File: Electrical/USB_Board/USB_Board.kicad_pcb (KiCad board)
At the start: 2 copper layers, 45 x 18 mm, 24 parts, among them J1 USB_B_Mini, Q1 BC850, Q2 BC850, U1 FT232RL, U2 AD8620

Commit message: Fixed hole size on ICSP board.
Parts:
- D1: footprint LED_SMD:LED_1206_3216Metric -> Diode_SMD:D_1206_3216Metric
- L4, L5: footprint Diode_SMD:D_1206_3216Metric -> LED_SMD:LED_1206_3216Metric

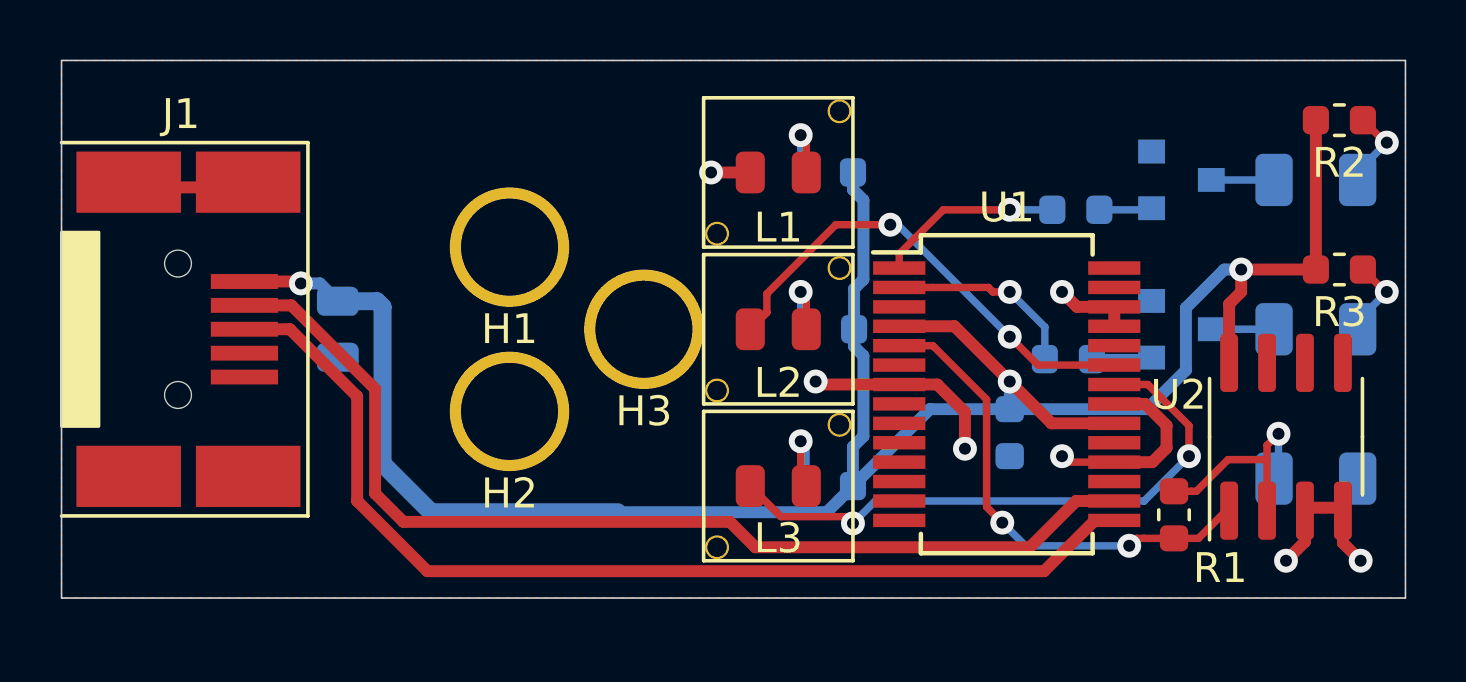
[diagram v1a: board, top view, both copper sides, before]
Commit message: Updated transimpedance amp and rearranged USB board.
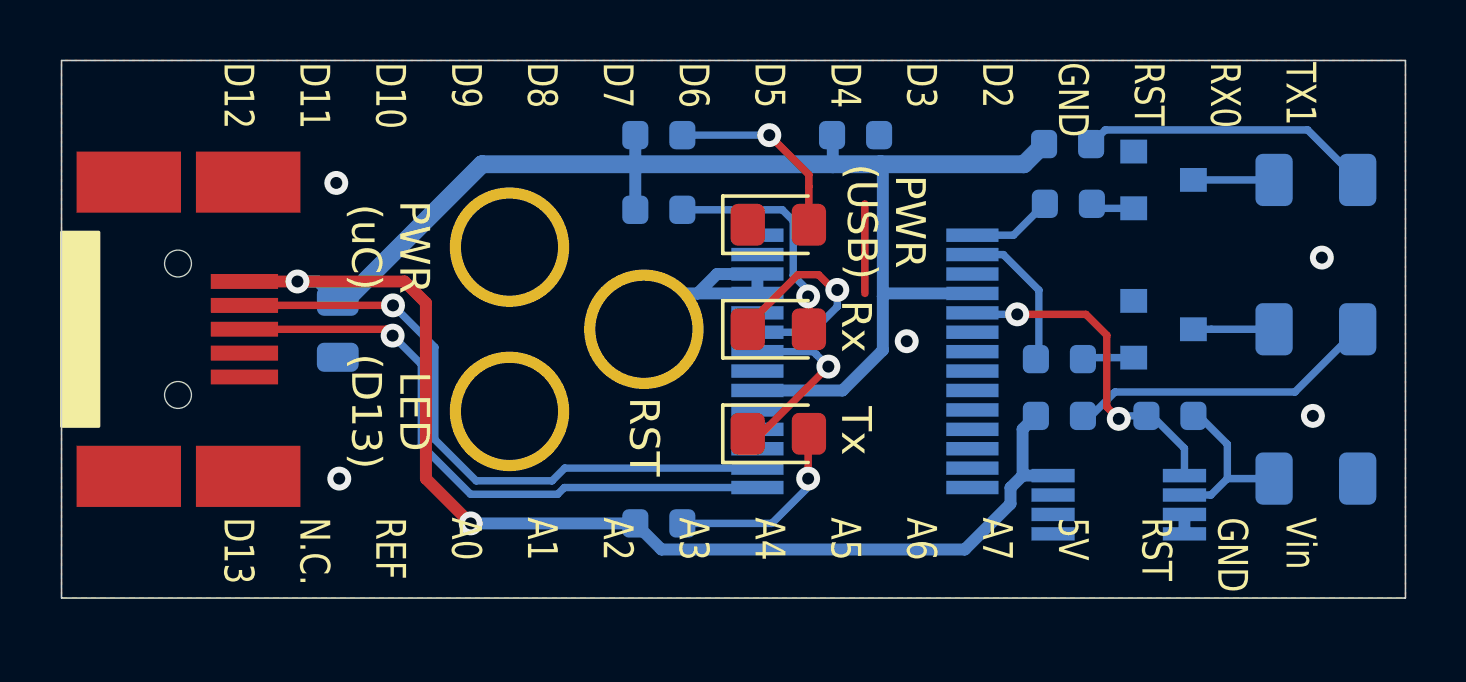
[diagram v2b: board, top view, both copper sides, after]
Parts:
- added REF**: ArdNanoLabels, hodgkin:ArdNanoLabels, F.Cu at (123.7, 100.2)
- L1, L2, L3: footprint hodgkin:LED_0805_LightPipe -> LED_SMD:LED_0805_2012Metric_Pad1.15x1.40mm_HandSolder
- R1, R2, U1: moved to B.Cu
- R5: renamed from R3; moved to B.Cu
- U2: value AD8620 -> OPA2381; footprint Package_SO:SOIC-8_3.9x4.9mm_P1.27mm -> Package_SO:MSOP-8_3x3mm_P0.65mm; moved to B.Cu
- moved C1 11.2 mm to (126.6, 93.5), turned to 0 degrees
- moved R5 10.6 mm to (133.4, 102.9)
- moved R2 9.14 mm to (133.7, 93.8)
- moved R7 7.00 mm to (120.0, 96.0), turned to 180 degrees
- moved U2 6.04 mm to (135.4, 105.9), turned to 180 degrees
- moved R6 5.85 mm to (120.0, 93.5), turned to 180 degrees
- moved R8 5.85 mm to (120.0, 106.5), turned to 180 degrees
- moved U1 4.88 mm to (126.9, 101.1), turned to 180 degrees
- moved R1 3.32 mm to (137.1, 102.9), turned to 0 degrees
- moved L1 1.75 mm to (124.0, 96.5)
- moved L3 1.75 mm to (124.0, 103.5)
- moved Q1 0.60 mm to (136.9, 95.0)
- moved Q2 0.60 mm to (136.9, 100.0)
- moved R3 0.32 mm to (133.7, 95.8)
- moved R4 0.30 mm to (133.4, 101.0)
- renumbered R4 to R3, R5 to R4
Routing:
- net GND: track 24.3 -> 7.87 mm, vias 7 -> 5
- net Net-(J1-Pad3): track 35.2 -> 21.1 mm, vias 0 -> 1
- net Net-(L3-Pad1): track 20.2 -> 6.22 mm, vias 2 -> 1
- net Net-(J1-Pad2): track 35.2 -> 21.6 mm, vias 0 -> 1
- net Net-(L2-Pad1): track 16.0 -> 7.65 mm, vias 2 -> 1
- net Net-(L5-Pad2): track 2.76 -> 10.1 mm, vias 1 -> 0
- net +5V: track 75.5 -> 82.8 mm, vias 3 -> 2
- net Net-(L4-Pad2): track 2.76 -> 9.82 mm, vias 1 -> 0
- net Net-(R1-Pad1): track 16.5 -> 11.4 mm
- net Net-(L2-Pad2): track 2.67 -> 7.73 mm
- net Net-(L1-Pad2): track 2.65 -> 6.46 mm
- net Net-(L3-Pad2): track 3.15 -> 6.51 mm
- net Net-(R3-Pad1): track 6.21 -> 2.90 mm, vias 1 -> 0
- net (no net): track 0.00 -> 3.00 mm
- net Net-(D1-Pad1): track 7.75 -> 5.91 mm, vias 1 -> 0
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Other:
- board text added: "LED (D13)"
- board text added: "PWR (USB)"
- board text added: "PWR (uC)"
- board text added: "RST"
- board text added: "Rx"
- board text added: "Tx"
